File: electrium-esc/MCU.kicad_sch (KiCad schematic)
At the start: 31 parts, among them J5 Debug Connector, SW1 SW_SPDT, U1 STM32F407ZGT6, Y1 25MHz

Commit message: Update footprints
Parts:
- J5: footprint Connector_PinHeader_2.54mm:PinHeader_1x06_P2.54mm_Horizontal -> Connector_PinHeader_2.54mm:PinHeader_1x06_P2.54mm_Vertical
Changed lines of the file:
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@@
     (property "Reference" "J5" (id 0) (at 185.42 92.71 0))
     (property "Value" "Debug Connector" (id 1) (at 181.61 111.76 0))
-    (property "Footprint" "Connector_PinHeader_2.54mm:PinHeader_1x06_P2.54mm_Horizontal" (id 2) (at 186.69 104.14 0)
+    (property "Footprint" "Connector_PinHeader_2.54mm:PinHeader_1x06_P2.54mm_Vertical" (id 2) (at 186.69 104.14 0)
       (effects (font (size 1.27 1.27)) hide)
     )

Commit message: relabel components to make more sense
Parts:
- renumbered C12 to C1, C11 to C10, C13 to C11, C16 to C12, C19 to C13, C22 to C14, C25 to C15, C14 to C16, C20 to C18, C23 to C19, C15 to C2, C2 to C20, C6 to C21, C8 to C22, C4 to C23, C5 to C24, C18 to C3, C21 to C4, C24 to C5, C3 to C6, C9 to C8, C10 to C9, J5 to J1, R15 to R1

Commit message: Change to cheaper mosfets
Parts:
- SW1: footprint Resistor_SMD:R_0603_1608Metric -> Button_Switch_THT:SW_CuK_JS202011CQN_DPDT_Straight
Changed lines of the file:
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@@
     (property "Reference" "SW1" (id 0) (at 46.99 64.77 0))
     (property "Value" "SW_SPDT" (id 1) (at 46.99 74.93 0))
-    (property "Footprint" "Resistor_SMD:R_0603_1608Metric" (id 2) (at 45.72 69.85 0)
+    (property "Footprint" "Button_Switch_THT:SW_CuK_JS202011CQN_DPDT_Straight" (id 2) (at 45.72 69.85 0)
       (effects (font (size 1.27 1.27)) hide)
     )

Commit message: Semi-finished schematic
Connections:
- net CS_B: now also U1.77 (PD8); no longer U1.74 (PB13)
- net DC_CAL_A: now also U1.99 (PC9); no longer U1.91 (PG6)
- net DC_CAL_B: now also U1.74 (PB13); no longer U1.88 (PG3)
- net EN_GATE_A: now also U1.98 (PC8); no longer U1.90 (PG5)
- net EN_GATE_B: now also U1.73 (PB12); no longer U1.87 (PG2)
- net H3_B: now also U1.46 (PB0); no longer U1.47 (PB1)
- net L3_B: now also U1.47 (PB1); no longer U1.46 (PB0)
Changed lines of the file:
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@@
   (no_connect (at 73.66 217.17))
   (no_connect (at 134.62 133.35))
+  (no_connect (at 73.66 118.11))
   (no_connect (at 73.66 105.41))
   (no_connect (at 73.66 199.39))
   (no_connect (at 73.66 133.35))
+  (no_connect (at 73.66 120.65))
   (no_connect (at 73.66 186.69))
   (no_connect (at 73.66 156.21))
@@
   (no_connect (at 73.66 143.51))
   (no_connect (at 134.62 209.55))
-  (no_connect (at 134.62 171.45))
   (no_connect (at 134.62 207.01))
   (no_connect (at 73.66 140.97))
-  (no_connect (at 134.62 212.09))
   (no_connect (at 134.62 85.09))
   (no_connect (at 73.66 222.25))
@@
   (no_connect (at 73.66 138.43))
   (no_connect (at 134.62 201.93))
-  (no_connect (at 134.62 135.89))
   (no_connect (at 134.62 125.73))
   (no_connect (at 73.66 184.15))
@@
   (no_connect (at 73.66 130.81))
   (no_connect (at 73.66 212.09))
+  (no_connect (at 73.66 110.49))
   (no_connect (at 73.66 179.07))
   (no_connect (at 73.66 229.87))
@@
   (no_connect (at 134.62 204.47))
   (no_connect (at 134.62 118.11))
+  (no_connect (at 73.66 113.03))
   (no_connect (at 73.66 204.47))
-  (no_connect (at 134.62 168.91))
   (no_connect (at 73.66 191.77))
   (no_connect (at 73.66 151.13))
@@
     (effects (font (size 1.27 1.27)) (justify right))
   )
-  (hierarchical_label "EN_GATE_A" (shape output) (at 73.66 118.11 180)
-    (effects (font (size 1.27 1.27)) (justify right))
+  (hierarchical_label "EN_GATE_A" (shape output) (at 134.62 168.91 0)
+    (effects (font (size 1.27 1.27)) (justify left))
   )
   (hierarchical_label "L3_A" (shape output) (at 134.62 222.25 0)
@@
     (effects (font (size 1.27 1.27)) (justify right))
   )
-  (hierarchical_label "DC_CAL_B" (shape output) (at 73.66 113.03 180)
-    (effects (font (size 1.27 1.27)) (justify right))
+  (hierarchical_label "DC_CAL_B" (shape output) (at 134.62 138.43 0)
+    (effects (font (size 1.27 1.27)) (justify left))
   )
   (hierarchical_label "SCK_A" (shape output) (at 134.62 173.99 0)
@@
     (effects (font (size 1.27 1.27)) (justify right))
   )
-  (hierarchical_label "CS_B" (shape output) (at 134.62 138.43 0)
-    (effects (font (size 1.27 1.27)) (justify left))
-  )
-  (hierarchical_label "L3_B" (shape output) (at 134.62 105.41 0)
+  (hierarchical_label "CS_B" (shape output) (at 134.62 212.09 0)
+    (effects (font (size 1.27 1.27)) (justify left))
+  )
+  (hierarchical_label "L3_B" (shape output) (at 134.62 107.95 0)
     (effects (font (size 1.27 1.27)) (justify left))
   )
@@
     (effects (font (size 1.27 1.27)) (justify right))
   )
-  (hierarchical_label "H3_B" (shape output) (at 134.62 107.95 0)
+  (hierarchical_label "H3_B" (shape output) (at 134.62 105.41 0)
     (effects (font (size 1.27 1.27)) (justify left))
   )
@@
     (effects (font (size 1.27 1.27)) (justify left))
   )
-  (hierarchical_label "EN_GATE_B" (shape output) (at 73.66 110.49 180)
-    (effects (font (size 1.27 1.27)) (justify right))
+  (hierarchical_label "EN_GATE_B" (shape output) (at 134.62 135.89 0)
+    (effects (font (size 1.27 1.27)) (justify left))
   )
   (hierarchical_label "TEMP_A" (shape input) (at 134.62 158.75 0)
@@
     (effects (font (size 1.27 1.27)) (justify left))
   )
-  (hierarchical_label "DC_CAL_A" (shape output) (at 73.66 120.65 180)
-    (effects (font (size 1.27 1.27)) (justify right))
+  (hierarchical_label "DC_CAL_A" (shape output) (at 134.62 171.45 0)
+    (effects (font (size 1.27 1.27)) (justify left))
   )
   (hierarchical_label "L2_A" (shape output) (at 134.62 227.33 0)

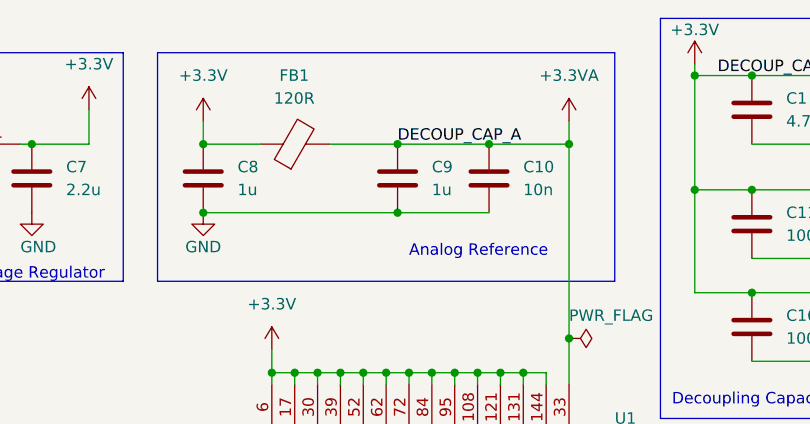
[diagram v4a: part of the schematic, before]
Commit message: Update more components and few traces
Final design hopefully done by tomorrow. Logistical problems are coming through, needs to suit components to those needs
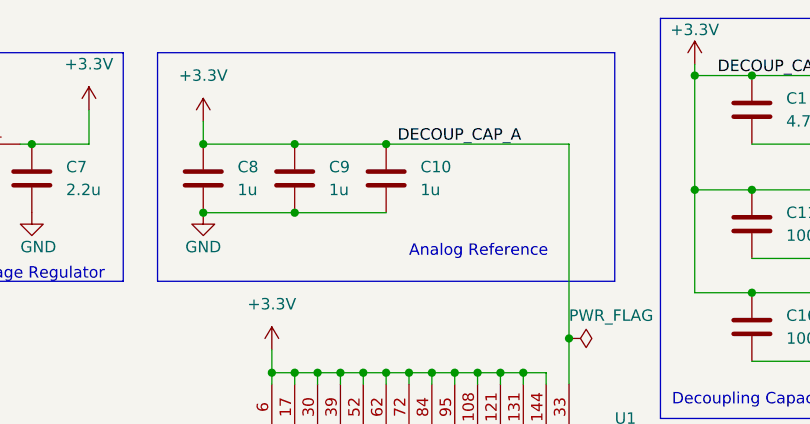
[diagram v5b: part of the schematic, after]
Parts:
- removed FB1: 120R, Ferrite_THT:LairdTech_28C0236-0JW-10, symbol Device:FerriteBead
- C10: value 10n -> 1u
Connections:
- net +3.3VA is gone; now on net +3.3V: C10.1, C9.1, U1.33 (VDDA)
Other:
- moved on the sheet: C10, C9
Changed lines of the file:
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@@
   (junction (at 187.96 40.64) (diameter 0) (color 0 0 0 0)
   )
+  (junction (at 91.44 35.56) (diameter 0) (color 0 0 0 0)
+  )
   (junction (at 22.86 120.65) (diameter 0) (color 0 0 0 0)
   )
@@
   (junction (at 99.06 238.76) (diameter 0) (color 0 0 0 0)
   )
-  (junction (at 121.92 27.94) (diameter 0) (color 0 0 0 0)
-  )
-  (junction (at 113.03 27.94) (diameter 0) (color 0 0 0 0)
-  )
   (junction (at 69.85 74.93) (diameter 0) (color 0 0 0 0)
   )
@@
   (junction (at 176.53 33.02) (diameter 0) (color 0 0 0 0)
   )
-  (junction (at 102.87 35.56) (diameter 0) (color 0 0 0 0)
-  )
   (junction (at 135.89 33.02) (diameter 0) (color 0 0 0 0)
   )
+  (junction (at 91.44 27.94) (diameter 0) (color 0 0 0 0)
+  )
   (junction (at 109.22 238.76) (diameter 0) (color 0 0 0 0)
   )
@@
   (junction (at 121.92 49.53) (diameter 0) (color 0 0 0 0)
   )
-  (junction (at 102.87 27.94) (diameter 0) (color 0 0 0 0)
-  )
   (junction (at 96.52 53.34) (diameter 0) (color 0 0 0 0)
   )
   (junction (at 62.23 27.94) (diameter 0) (color 0 0 0 0)
+  )
+  (junction (at 101.6 27.94) (diameter 0) (color 0 0 0 0)
   )
   (junction (at 93.98 238.76) (diameter 0) (color 0 0 0 0)
@@
     (stroke (width 0) (type default) (color 0 0 0 0))
   )
+  (wire (pts (xy 101.6 27.94) (xy 121.92 27.94))
+    (stroke (width 0) (type default) (color 0 0 0 0))
+  )
   (wire (pts (xy 114.3 238.76) (xy 116.84 238.76))
     (stroke (width 0) (type default) (color 0 0 0 0))
@@
     (stroke (width 0) (type default) (color 0 0 0 0))
   )
+  (wire (pts (xy 91.44 35.56) (xy 101.6 35.56))
+    (stroke (width 0) (type default) (color 0 0 0 0))
+  )
   (wire (pts (xy 142.24 20.32) (xy 153.67 20.32))
     (stroke (width 0) (type default) (color 0 0 0 0))
@@
     (stroke (width 0) (type default) (color 0 0 0 0))
   )
-  (wire (pts (xy 95.25 27.94) (xy 102.87 27.94))
-    (stroke (width 0) (type default) (color 0 0 0 0))
-  )
   (wire (pts (xy 142.24 40.64) (xy 153.67 40.64))
     (stroke (width 0) (type default) (color 0 0 0 0))
@@
     (stroke (width 0) (type default) (color 0 0 0 0))
   )
-  (wire (pts (xy 121.92 27.94) (xy 113.03 27.94))
-    (stroke (width 0) (type default) (color 0 0 0 0))
-  )
   (wire (pts (xy 25.4 26.67) (xy 25.4 27.94))
     (stroke (width 0) (type default) (color 0 0 0 0))
@@
     (stroke (width 0) (type default) (color 0 0 0 0))
   )
-  (wire (pts (xy 121.92 25.4) (xy 121.92 27.94))
-    (stroke (width 0) (type default) (color 0 0 0 0))
-  )
   (polyline (pts (xy 127 17.78) (xy 127 43.18))
     (stroke (width 0) (type default) (color 0 0 0 0))
@@
     (stroke (width 0) (type default) (color 0 0 0 0))
   )
-  (wire (pts (xy 81.28 27.94) (xy 87.63 27.94))
+  (wire (pts (xy 81.28 27.94) (xy 91.44 27.94))
     (stroke (width 0) (type default) (color 0 0 0 0))
   )
@@
     (stroke (width 0) (type default) (color 0 0 0 0))
   )
-  (wire (pts (xy 81.28 35.56) (xy 102.87 35.56))
+  (wire (pts (xy 81.28 35.56) (xy 91.44 35.56))
     (stroke (width 0) (type default) (color 0 0 0 0))
   )
@@
     (stroke (width 0) (type default) (color 0 0 0 0))
   )
-  (wire (pts (xy 102.87 35.56) (xy 113.03 35.56))
-    (stroke (width 0) (type default) (color 0 0 0 0))
-  )
   (wire (pts (xy 50.8 69.85) (xy 58.42 69.85))
     (stroke (width 0) (type default) (color 0 0 0 0))
@@
     (stroke (width 0) (type default) (color 0 0 0 0))
   )
-  (wire (pts (xy 113.03 27.94) (xy 102.87 27.94))
+  (wire (pts (xy 91.44 27.94) (xy 101.6 27.94))
     (stroke (width 0) (type default) (color 0 0 0 0))
   )
@@
     (pin "2")
   )
-  (symbol (lib_id "Device:FerriteBead") (at 91.44 27.94 90) (unit 1)
-    (in_bom yes) (on_board yes) (fields_autoplaced)
-    (property "Reference" "FB1" (id 0) (at 91.3892 20.32 90))
-    (property "Value" "120R" (id 1) (at 91.3892 22.86 90))
-    (property "Footprint" "Ferrite_THT:LairdTech_28C0236-0JW-10" (id 2) (at 91.44 29.718 90)
-      (effects (font (size 1.27 1.27)) hide)
-    )
-    (property "Datasheet" "~" (id 3) (at 91.44 27.94 0)
-      (effects (font (size 1.27 1.27)) hide)
-    )
-    (pin "1")
-    (pin "2")
-  )
   (symbol (lib_id "power:GND") (at 25.4 24.13 180) (unit 1)
     (in_bom yes) (on_board yes) (fields_autoplaced)
@@
     (pin "2")
   )
-  (symbol (lib_id "Device:C") (at 113.03 31.75 0) (unit 1)
-    (in_bom yes) (on_board yes) (fields_autoplaced)
-    (property "Reference" "C10" (id 0) (at 116.84 30.4799 0)
-      (effects (font (size 1.27 1.27)) (justify left))
-    )
-    (property "Value" "10n" (id 1) (at 116.84 33.0199 0)
-      (effects (font (size 1.27 1.27)) (justify left))
-    )
-    (property "Footprint" "Capacitor_SMD:C_0603_1608Metric" (id 2) (at 113.9952 35.56 0)
-      (effects (font (size 1.27 1.27)) hide)
-    )
-    (property "Datasheet" "~" (id 3) (at 113.03 31.75 0)
+  (symbol (lib_id "Device:C") (at 101.6 31.75 0) (unit 1)
+    (in_bom yes) (on_board yes) (fields_autoplaced)
+    (property "Reference" "C10" (id 0) (at 105.41 30.4799 0)
+      (effects (font (size 1.27 1.27)) (justify left))
+    )
+    (property "Value" "1u" (id 1) (at 105.41 33.0199 0)
+      (effects (font (size 1.27 1.27)) (justify left))
+    )
+    (property "Footprint" "Capacitor_SMD:C_0603_1608Metric" (id 2) (at 102.5652 35.56 0)
+      (effects (font (size 1.27 1.27)) hide)
+    )
+    (property "Datasheet" "~" (id 3) (at 101.6 31.75 0)
       (effects (font (size 1.27 1.27)) hide)
     )
@@
     (pin "2")
   )
-  (symbol (lib_id "power:+3.3VA") (at 121.92 25.4 0) (unit 1)
-    (in_bom yes) (on_board yes) (fields_autoplaced)
-    (property "Reference" "#PWR05" (id 0) (at 121.92 29.21 0)
-      (effects (font (size 1.27 1.27)) hide)
-    )
-    (property "Value" "+3.3VA" (id 1) (at 121.92 20.32 0))
-    (property "Footprint" "" (id 2) (at 121.92 25.4 0)
-      (effects (font (size 1.27 1.27)) hide)
-    )
-    (property "Datasheet" "" (id 3) (at 121.92 25.4 0)
-      (effects (font (size 1.27 1.27)) hide)
-    )
-    (pin "1")
-  )
   (symbol (lib_id "power:+3.3V") (at 135.89 19.05 0) (unit 1)
     (in_bom yes) (on_board yes)
@@
     (pin "1")
   )
-  (symbol (lib_id "Device:C") (at 102.87 31.75 0) (unit 1)
-    (in_bom yes) (on_board yes) (fields_autoplaced)
-    (property "Reference" "C9" (id 0) (at 106.68 30.4799 0)
-      (effects (font (size 1.27 1.27)) (justify left))
-    )
-    (property "Value" "1u" (id 1) (at 106.68 33.0199 0)
-      (effects (font (size 1.27 1.27)) (justify left))
-    )
-    (property "Footprint" "Capacitor_SMD:C_0603_1608Metric" (id 2) (at 103.8352 35.56 0)
-      (effects (font (size 1.27 1.27)) hide)
-    )
-    (property "Datasheet" "~" (id 3) (at 102.87 31.75 0)
-      (effects (font (size 1.27 1.27)) hide)
-    )
+  (symbol (lib_id "Device:C") (at 91.44 31.75 0) (unit 1)
+    (in_bom yes) (on_board yes) (fields_autoplaced)
+    (property "Reference" "C9" (id 0) (at 95.25 30.4799 0)
+      (effects (font (size 1.27 1.27)) (justify left))
+    )
+    (property "Value" "1u" (id 1) (at 95.25 33.0199 0)
+      (effects (font (size 1.27 1.27)) (justify left))
+    )
+    (property "Footprint" "Capacitor_SMD:C_0603_1608Metric" (id 2) (at 92.4052 35.56 0)
+      (effects (font (size 1.27 1.27)) hide)
+    )
+    (property "Datasheet" "~" (id 3) (at 91.44 31.75 0)
+      (effects (font (size 1.27 1.27)) hide)
+    )
